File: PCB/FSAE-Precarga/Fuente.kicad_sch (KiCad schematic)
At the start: 5 parts, among them U1 SPAN02E-12, U7 LM1117DT-3.3

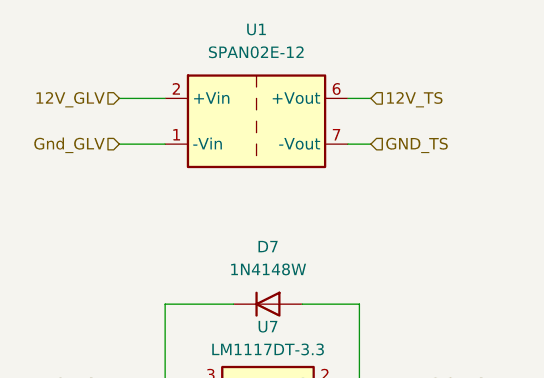
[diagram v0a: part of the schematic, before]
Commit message: Version avanzada de la placa de Precarga
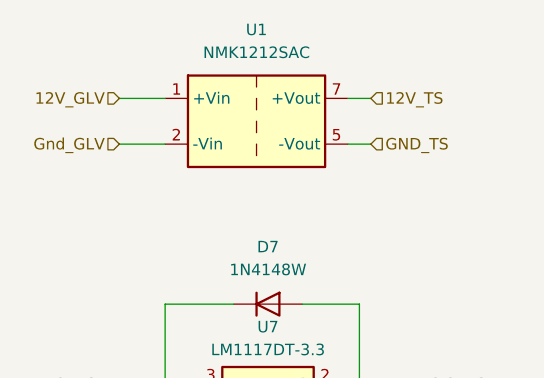
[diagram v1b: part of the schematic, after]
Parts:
- U1: value SPAN02E-12 -> NMK1212SAC; footprint Mis_Huellas:SPAN02E-12 -> Mis_Huellas:NMK0512SAC; PaginaProveedor https://www.digikey.com/en/products/detail/mean-well-usa-in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 -> https://www.digikey.com/en/products/detail/murata-power-sol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
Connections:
- net 12V_GLV: now also U1.1 (+Vin); no longer U1.2 (+Vin)
- net 12V_TS: now also U1.7 (+Vout); no longer U1.6 (+Vout)
- net GND_TS: now also U1.5 (-Vout); no longer U1.7 (-Vout)
- net Gnd_GLV: now also U1.2 (-Vin); no longer U1.1 (-Vin)
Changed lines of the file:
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@@
 			)
 		)
-		(property "Value" "SPAN02E-12"
+		(property "Value" "NMK1212SAC"
 			(at 152.4 54.61 0)
 			(effects
@@
 			)
 		)
-		(property "Footprint" "Mis_Huellas:SPAN02E-12"
+		(property "Footprint" "Mis_Huellas:NMK0512SAC"
 			(at 152.4 71.12 0)
 			(effects
@@
 			)
 		)
-		(property "Datasheet" "https://mm.digikey.com/Volume0/opasdata/d220001/medias/docus/2127/SPAN02%2CDPAN02_Series_Ds.pdf"
+		(property "Datasheet" "https://pim.murata.com/asset/pim4/isolatedDCDCconverter/KDC_NMK_PDF_ISOLATEDDCDCCONVERTER?lastModifiedDatetime=20250707193448"
 			(at 152.4 68.58 0)
 			(effects
@@
 			)
 		)
-		(property "Description" "1W DC/DC converter unregulated, 10.8-13.2V input, 12V fixed output voltage, 84mA output, 1.0kVDC isolation, SIP-7"
+		(property "Description" "DC DC CONVERTER 12V 2W"
 			(at 152.4 62.23 0)
 			(effects
@@
 			)
 		)
-		(property "PaginaProveedor" "https://www.digikey.com/en/products/detail/mean-well-usa-inc/SPAN02E-12/7706979"
+		(property "PaginaProveedor" "https://www.digikey.com/en/products/detail/murata-power-solutions-inc/NMK1212SAC/1927113"
 			(at 152.4 62.23 0)
 			(effects
@@
 			)
 		)
-		(pin "6"
+		(pin "5"
 		)
 		(pin "7"

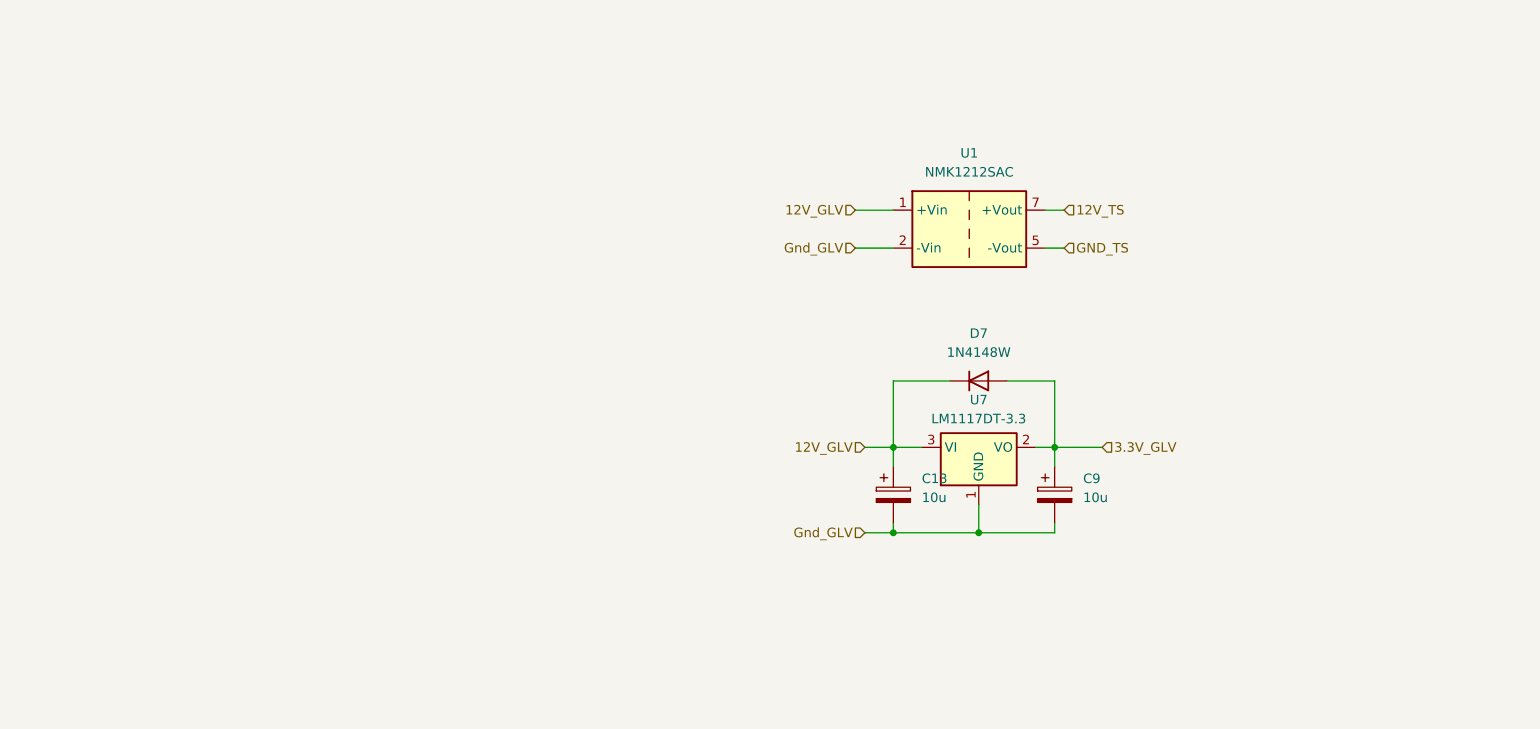
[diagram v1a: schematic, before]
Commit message: Subo correcciones placa de precarga
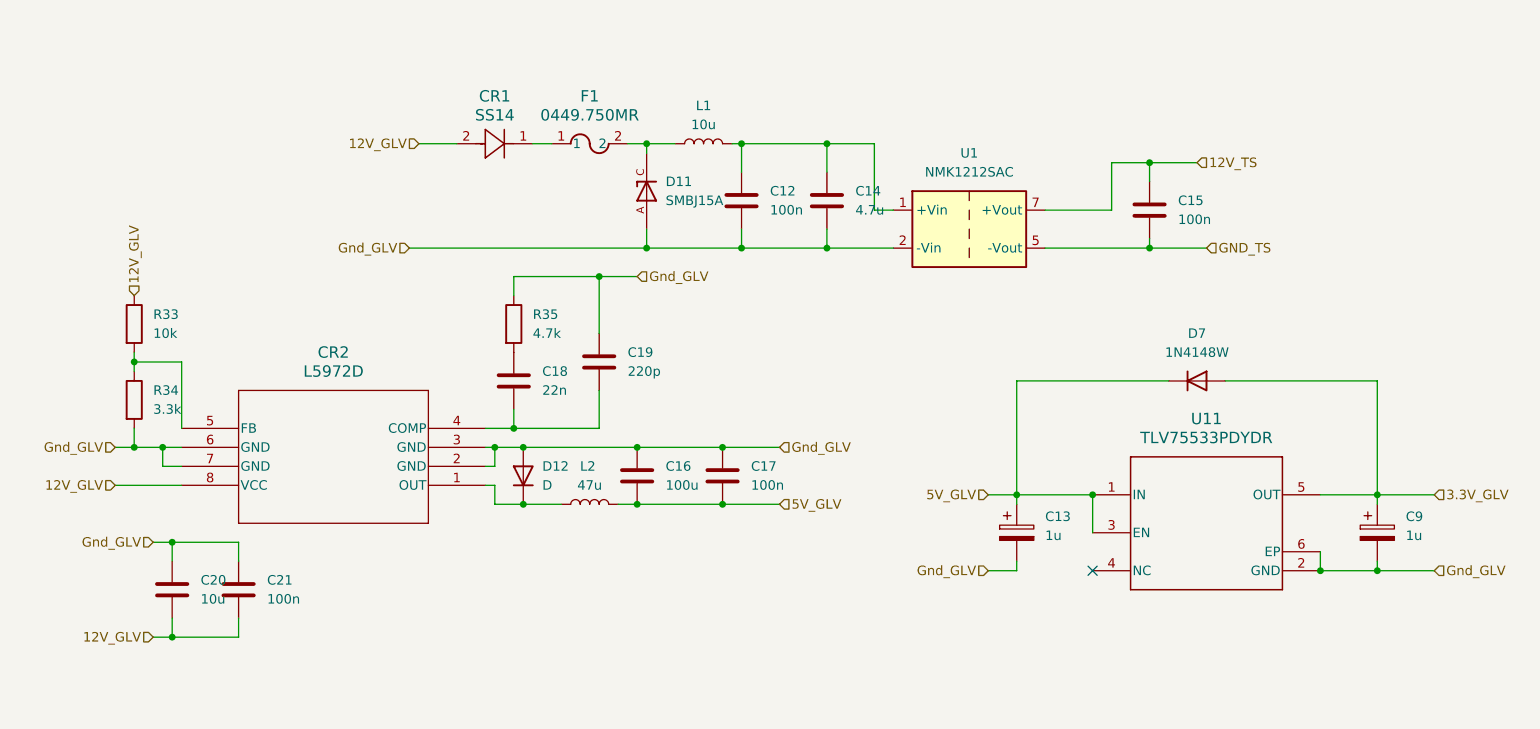
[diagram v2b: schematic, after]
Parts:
- removed U7: LM1117DT-3.3, Package_TO_SOT_SMD:TO-252-2, symbol Regulator_Linear:LM1117DT-3.3
- added C12, C15, C17, C21: 100n, symbol Device:C
- added C14: 4.7u, symbol Device:C
- added C16: 100u, symbol Device:C
- added C18: 22n, symbol Device:C
- added C19: 220p, symbol Device:C
- added C20: 10u, symbol Device:C
- added CR1: SS14, CR_SMA_403AE_OSI, symbol 2026-08-25_19-36-53:SS14
- added CR2: L5972D, SO-8_STM, symbol 2026-08-26_03-53-17:L5972D
- added D11: SMBJ15A, SMBJ15A:DIOM4336X265N, symbol SMBJ15A:SMBJ15A
- added D12: D, symbol Device:D
- added F1: 0449.750MR, 0449Series_LTF, symbol 2026-08-26_15-02-46:0449.750MR
- added L1: 10u, symbol Device:L
- added L2: 47u, symbol Device:L
- added R33: 10k, symbol Device:R
- added R34: 3.3k, symbol Device:R
- added R35: 4.7k, symbol Device:R
- added U11: TLV75533PDYDR, DYD0005A-MFG, symbol 2026-08-26_04-16-45:TLV75533PDYDR
- C13, C9: value 10u -> 1u
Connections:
- net 12V_GLV: now also C20.2, C21.2, CR1.2, CR2.8 (VCC), R33.1; no longer C13.1, D7.1 (K), U1.1 (+Vin)
- net 12V_TS: now also C15.1
- net 3.3V_GLV: now also U11.5 (OUT)
- net GND_TS: now also C15.2
- net Gnd_GLV: now also C12.2, C14.2, C16.1, C17.1, C19.1, C20.1, C21.1, CR2.2 (GND), CR2.3 (GND), CR2.6 (GND), CR2.7 (GND), D11.A, D12.2 (A), R34.2, R35.1, U11.2 (GND), U11.6 (EP)
- new net: C18.2, C19.2, CR2.4 (COMP)
- new net: C18.1, R35.2
- new net: C12.1, C14.1, L1.2, U1.1 (+Vin)
- new net: CR2.1 (OUT), D12.1 (K), L2.1
- new net: CR2.5 (FB), R33.2, R34.1
- new net: CR1.1, F1.1
- new net: D11.C, F1.2, L1.1
- new net 5V_GLV: C13.1, C16.2, C17.2, D7.1 (K), L2.2, U11.1 (IN), U11.3 (EN)
- no-connect marks 0 -> 1
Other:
- moved on the sheet: C13, C9, D7

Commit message: Agrego correcciones/agregados placa precarga
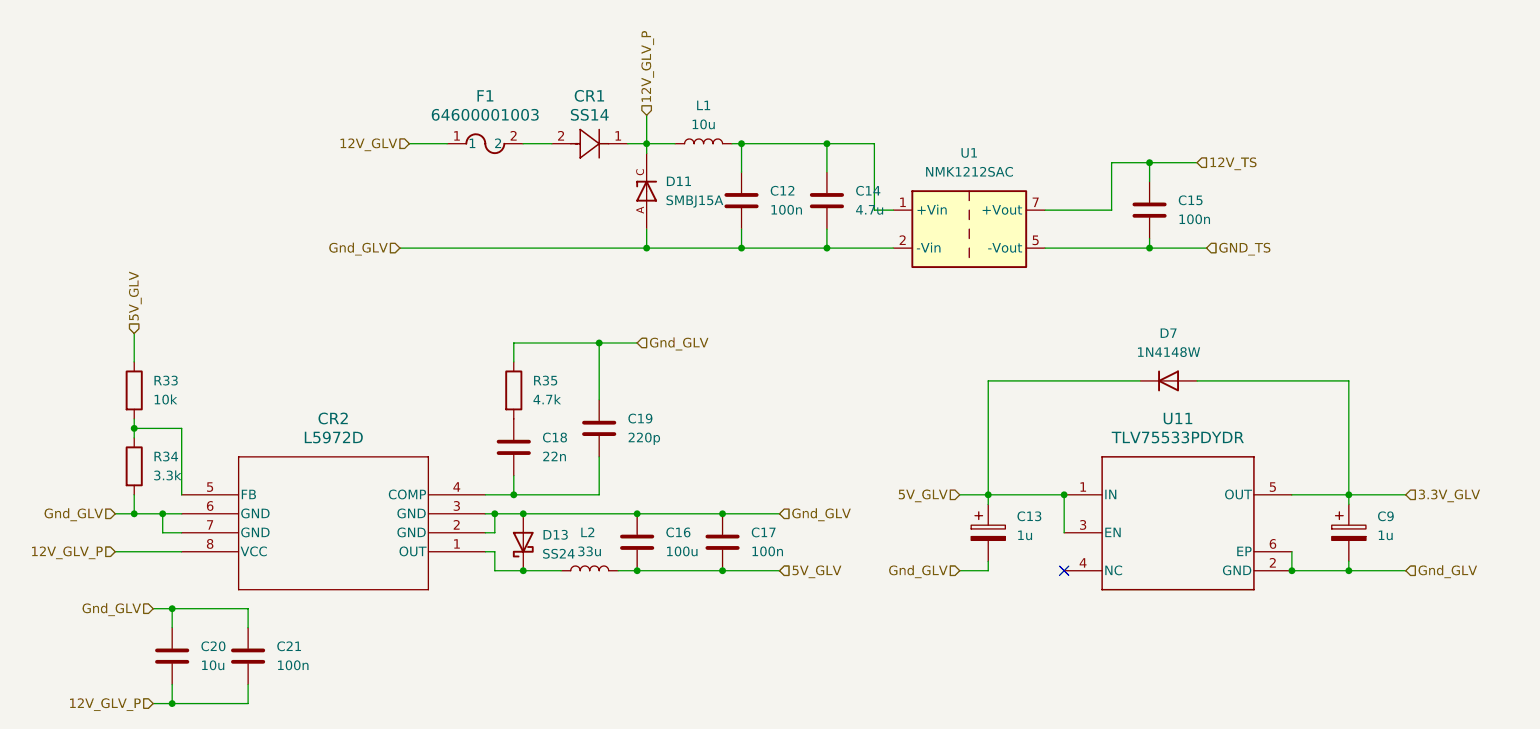
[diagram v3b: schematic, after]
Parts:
- removed D12: D, symbol Device:D
- removed F1: 0449.750MR, 0449Series_LTF, symbol 2026-08-26_15-02-46:0449.750MR
- added D13: SS24, Diode_SMD:D_SMA, symbol Diode:SS24
- added F1: 64600001003, Mis_Huellas:FUSE_646_1_LTF, symbol 2026-09-11_13-51-41:64600001003
- C12, C17, C21: footprint (none) -> Capacitor_SMD:C_0805_2012Metric; JLCPart (none) -> C53084462; PaginaProveedor (none) -> https://jlcpcb.com/partdetail/TORCH-CC0805X7R25V104KN/C5308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
- C14: footprint (none) -> Capacitor_SMD:C_0805_2012Metric; JLCPart (none) -> C162427; PaginaProveedor (none) -> https://jlcpcb.com/partdetail/173808-GRM21BR71E475KA73L/C16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
- C15: footprint (none) -> Capacitor_SMD:C_0805_2012Metric; JLCPart (none) -> C53084462; PaginaProveedor (none) -> http://jlcpcb.com/partdetail/TORCH-CC0805X7R25V104KN/C53084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
- C18: footprint (none) -> Capacitor_SMD:C_0805_2012Metric; JLCPart (none) -> C1729; PaginaProveedor (none) -> https://jlcpcb.com/partdetail/2081-CL21B223KBANNNC/C1729
- C19: footprint (none) -> Capacitor_SMD:C_0805_2012Metric; JLCPart (none) -> C22470019; PaginaProveedor (none) -> https://jlcpcb.com/partdetail/HRE-CGA0805C0G221J500HT/C2247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
- C20: footprint (none) -> Capacitor_SMD:C_0805_2012Metric; JLCPart (none) -> C237493; PaginaProveedor (none) -> https://jlcpcb.com/partdetail/236937-GRM21BZ71E106KE15L/C23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
- CR2: footprint SO-8_STM -> Mis_Huellas:SO-8_STM
- D11: footprint SMBJ15A:DIOM4336X265N -> Mis_Huellas:DIOM4336X265N
- L1: JLCPart (none) -> C237599; PaginaProovedor (none) -> https://jlcpcb.com/partdetail/MurataElectronics-1239AS_H_10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
- L2: value 47u -> 33u; footprint (none) -> Inductor_SMD:L_Chilisin_BMRB00060624; JLCPart (none) -> C5189937; PaginaProveedor (none) -> https://jlcpcb.com/partdetail/SHOUHAN-CYA065033UH/C5189937
- R33: footprint (none) -> Resistor_SMD:R_0805_2012Metric; JLCPart (none) -> C84376; PaginaProveedor (none) -> https://jlcpcb.com/partdetail/YAGEO-RC0805FR0710KL/C84376
- R34: footprint (none) -> Resistor_SMD:R_0805_2012Metric; JLCPart (none) -> C114531; PaginaProveedor (none) -> https://jlcpcb.com/partdetail/YAGEO-RC0805FR073K3L/C114531
- R35: footprint (none) -> Resistor_SMD:R_0805_2012Metric; JLCPart (none) -> C60816; PaginaProveedor (none) -> https://jlcpcb.com/partdetail/YAGEO-RC0805FR074K7L/C60816
- U11: footprint DYD0005A-MFG -> Mis_Huellas:DYD0005A-MFG
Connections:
- net 12V_GLV: now also F1.1; no longer C20.2, C21.2, CR1.2, CR2.8 (VCC), R33.1
- net 5V_GLV: now also R33.1
- net Gnd_GLV: now also D13.2 (A)
- net at CR2.1 (OUT), L2.1: now also D13.1 (K)
- net 12V_GLV_P: now reaches CR1.1
- net 12V_GLV_P: now also C20.2, C21.2, CR2.8 (VCC), D11.C, L1.1
- new net: CR1.2, F1.2
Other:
- moved on the sheet: C13, C16, C17, C18, C19, C20, C21, C9, CR1, CR2, D7, L2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
